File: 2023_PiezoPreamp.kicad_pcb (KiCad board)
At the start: 4 copper layers, 71 x 38 mm, 90 parts, among them J101 6.3mm stereo, J102 6.3mm stereo, J201 DC IN 5.5/2.1mm, J401 Spring Contact, U101 OPA145, U102 OPA145, U201 ZXMP3A17E6TA, U301 BC847BS,115

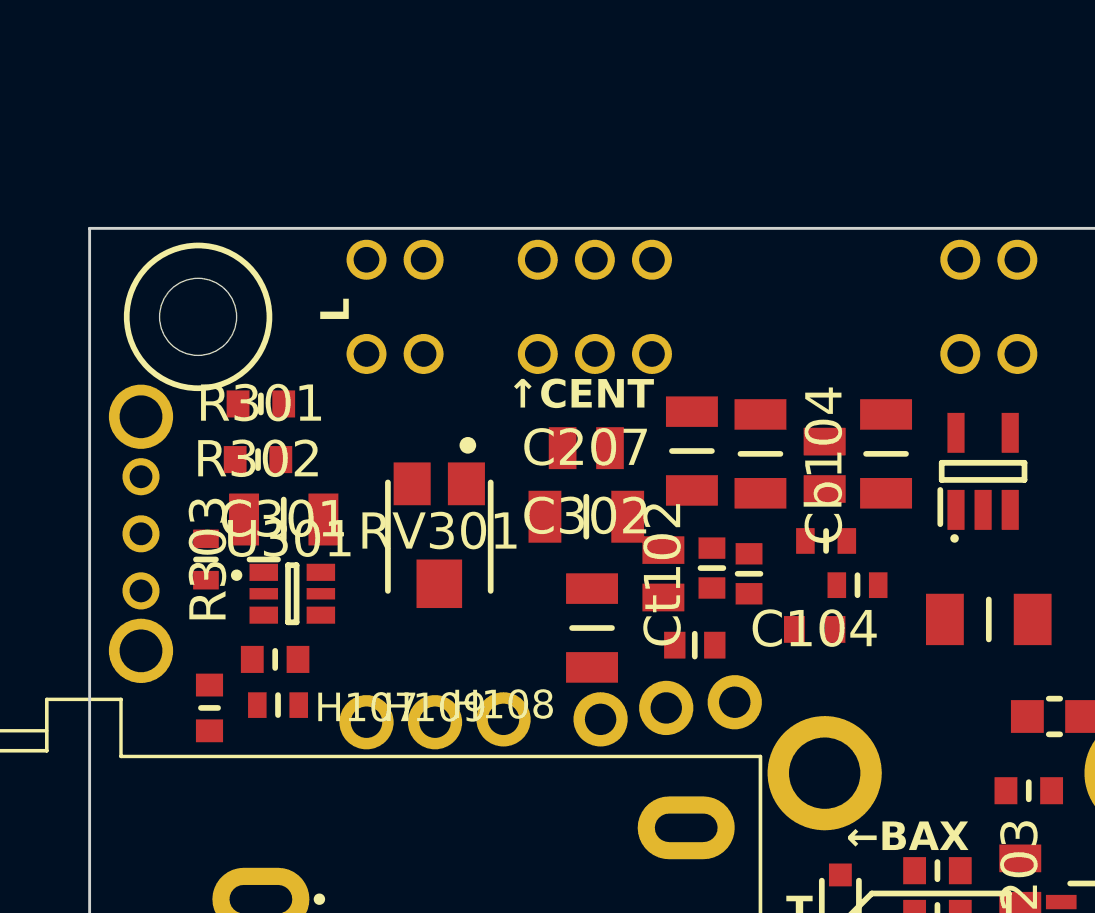
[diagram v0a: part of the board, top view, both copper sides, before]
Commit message: aligning schematics to grid, swapping switches as they are on the bottom side now; rough placement of BI section on board
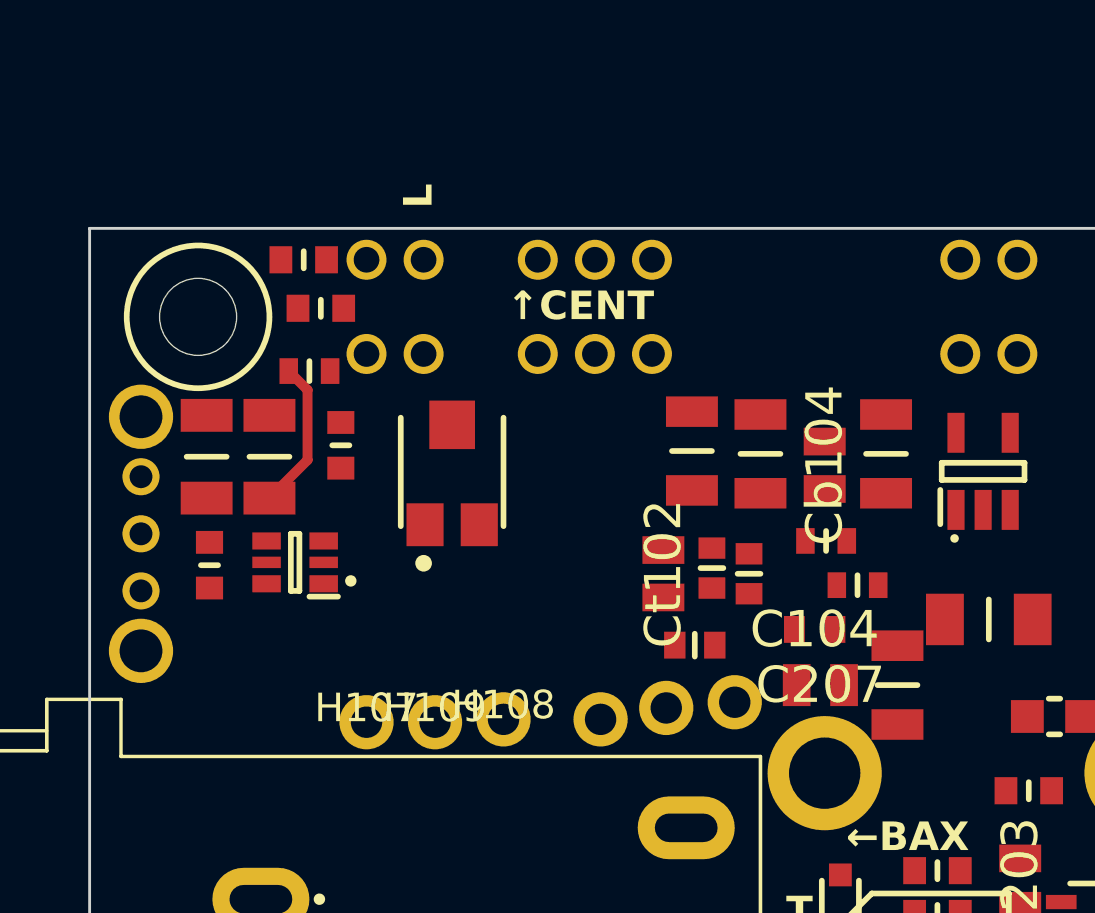
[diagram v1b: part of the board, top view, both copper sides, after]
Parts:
- removed the R304 at (121.5, 91.8)
- moved C207 11.7 mm to (140.5, 91.0)
- moved C302 11.3 mm to (121.2, 83.0), turned to -90 degrees
- moved C206 10.9 mm to (143.2, 91.0)
- moved R305 10.3 mm to (123.7, 82.7), turned to -90 degrees
- moved R303 7.53 mm to (122.6, 80.0), turned to 0 degrees
- moved R302 5.74 mm to (123.0, 77.8)
- moved R301 5.27 mm to (122.4, 76.2)
- moved R304 4.02 mm to (119.1, 86.8), turned to 90 degrees
- moved C301 3.48 mm to (119.0, 83.0), turned to -90 degrees
- moved RV301 2.31 mm to (127.6, 83.6), turned to 0 degrees
- moved U301 1.10 mm to (122.1, 86.8), turned to 180 degrees
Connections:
- Cb102 pad 1: /1-ChargeAmpAndEQ/C_SW_5 -> /1-ChargeAmpAndEQ/C_SW_1
- Cb103 pad 1: /1-ChargeAmpAndEQ/C_SW_4 -> /1-ChargeAmpAndEQ/C_SW_2
- Cb104 pad 1: /1-ChargeAmpAndEQ/C_SW_2 -> /1-ChargeAmpAndEQ/C_SW_4
- Cf102 pad 2: /1-ChargeAmpAndEQ/G_SW_6 -> /1-ChargeAmpAndEQ/G_SW_10
- Cf103 pad 2: /1-ChargeAmpAndEQ/G_SW_7 -> /1-ChargeAmpAndEQ/G_SW_9
- Cf104 pad 2: /1-ChargeAmpAndEQ/G_SW_7 -> /1-ChargeAmpAndEQ/G_SW_9
- Cf105 pad 2: /1-ChargeAmpAndEQ/G_SW_9 -> /1-ChargeAmpAndEQ/G_SW_7
- Cf106 pad 2: /1-ChargeAmpAndEQ/G_SW_10 -> /1-ChargeAmpAndEQ/G_SW_6
- Clp103 pad 1: /1-ChargeAmpAndEQ/LPF_SW_6 -> /1-ChargeAmpAndEQ/LPF_SW_10
- Clp104 pad 2: /1-ChargeAmpAndEQ/LPF_SW_7 -> /1-ChargeAmpAndEQ/LPF_SW_9
- Clp105 pad 2: /1-ChargeAmpAndEQ/LPF_SW_7 -> /1-ChargeAmpAndEQ/LPF_SW_9
- Clp106 pad 2: /1-ChargeAmpAndEQ/LPF_SW_9 -> /1-ChargeAmpAndEQ/LPF_SW_7
- Ct102 pad 2: /1-ChargeAmpAndEQ/C_SW_6 -> /1-ChargeAmpAndEQ/C_SW_10
- Ct103 pad 2: /1-ChargeAmpAndEQ/C_SW_7 -> /1-ChargeAmpAndEQ/C_SW_9
- Ct104 pad 2: /1-ChargeAmpAndEQ/C_SW_9 -> /1-ChargeAmpAndEQ/C_SW_7
- H101 pad 1: /1-ChargeAmpAndEQ/BA_1 -> /1-ChargeAmpAndEQ/BASS_1
- H102 pad 1: /1-ChargeAmpAndEQ/BA_2 -> /1-ChargeAmpAndEQ/BASS_2
- H103 pad 1: /1-ChargeAmpAndEQ/BA_3 -> /1-ChargeAmpAndEQ/BASS_3
- H104 pad 1: /1-ChargeAmpAndEQ/TR_1 -> /1-ChargeAmpAndEQ/TREB_1
- H105 pad 1: /1-ChargeAmpAndEQ/TR_2 -> /1-ChargeAmpAndEQ/TREB_2
- H106 pad 1: /1-ChargeAmpAndEQ/TR_3 -> /1-ChargeAmpAndEQ/TREB_3
- S102 pad 10: unconnected-(S102-Pad10) -> /1-ChargeAmpAndEQ/LPF_SW_10
- S102 pad 6: /1-ChargeAmpAndEQ/LPF_SW_6 -> unconnected-(S102-Pad6)
- S103 pad 1: unconnected-(S103-Pad1) -> /1-ChargeAmpAndEQ/C_SW_1
- S103 pad 10: unconnected-(S103-Pad10) -> /1-ChargeAmpAndEQ/C_SW_10
- S103 pad 5: /1-ChargeAmpAndEQ/C_SW_5 -> unconnected-(S103-Pad5)
- S103 pad 6: /1-ChargeAmpAndEQ/C_SW_6 -> unconnected-(S103-Pad6)
- S301 pad 1: unconnected-(S301-Pad1) -> /3-BatteryIndicator/BI_SW
- S301 pad 3: /3-BatteryIndicator/BI_SW -> unconnected-(S301-Pad3)
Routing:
- net /3-BatteryIndicator/BI_B1: track 0.00 -> 5.28 mm

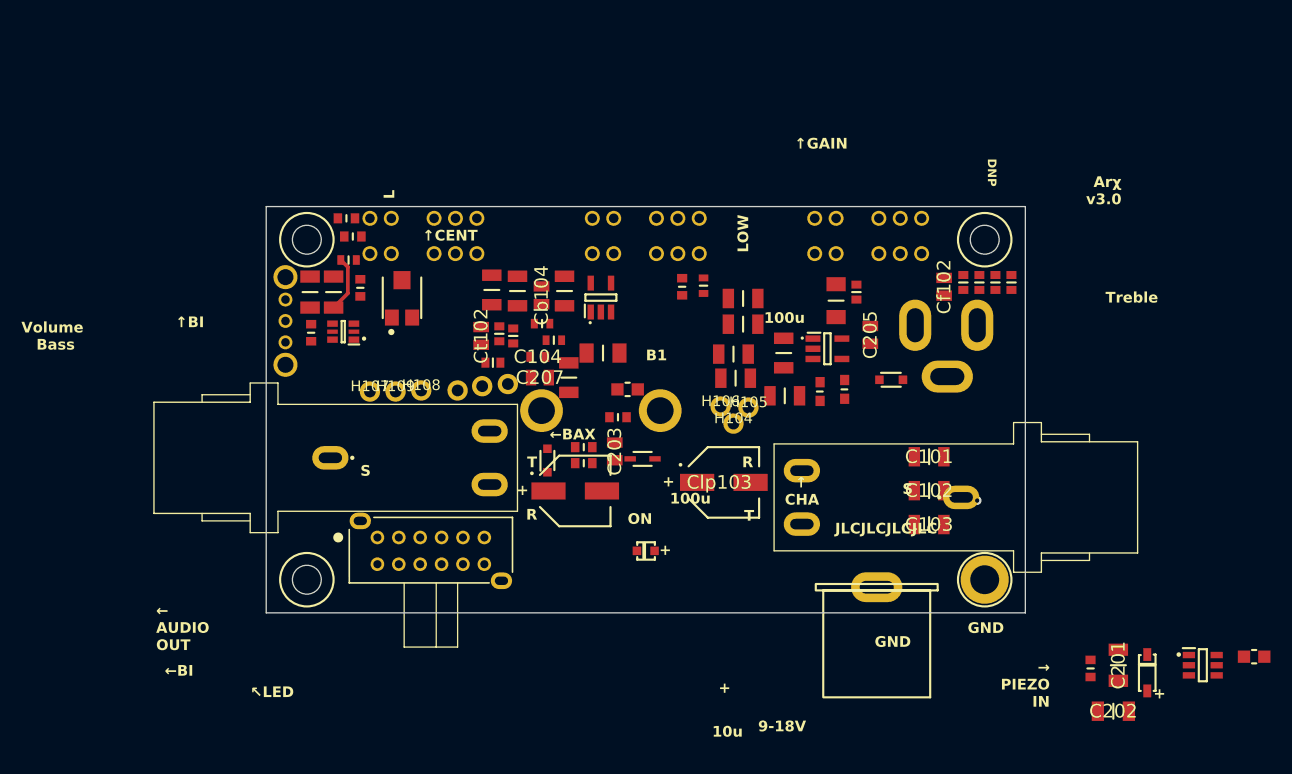
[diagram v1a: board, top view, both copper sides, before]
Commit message: PCB: updating all component footprints from schematics; starting some basic placement again
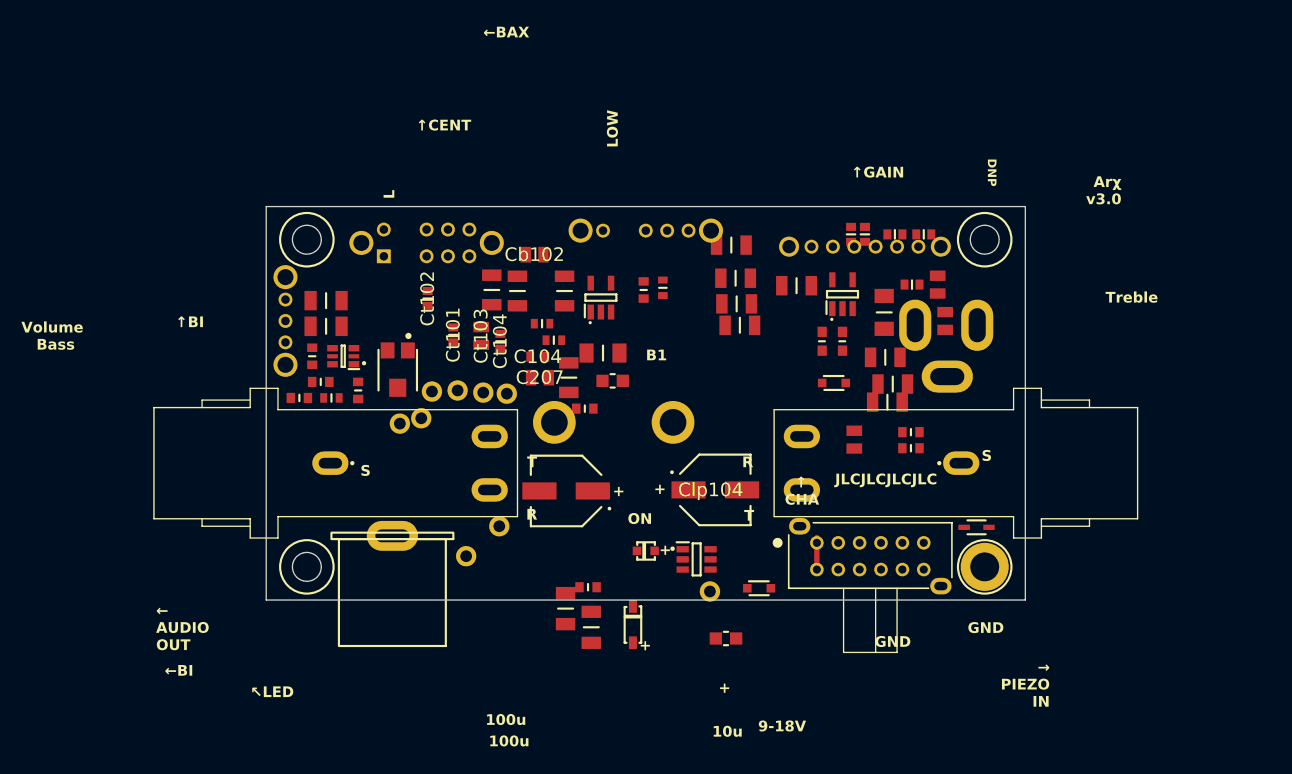
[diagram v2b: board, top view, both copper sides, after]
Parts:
- removed the Cb104 at (140.7, 83.3)
- removed the Clp104 at (159.5, 86.0)
- removed the Ct103 at (136.7, 87.0)
- added Cb102: 22n, library:GRM21B5C1H223JA01L, F.Cu at (140.0, 79.5)
- added Ct102: 4n7, library:GRM1885C1H472JA01D, F.Cu at (130.0, 83.7)
- Ct101: value 6n8 -> 4n7; footprint library:GRM1885C1H682JA01D -> library:GRM1885C1H472JA01D
- S101: value SSSS224100 -> SK14D01G6; footprint library:SSSS224100 -> library:sw_SK14D01G6
- S102: value SSSS224100 -> OS103011MA7QP1; footprint library:SSSS224100 -> library:sw_OS103011MA7QP1
- S103: value SSSS224100 -> 0S203011MA2QP1; footprint library:SSSS224100 -> library:sw_0S203011MA2QP1
- moved C202 52.1 mm to (142.9, 112.7), turned to -90 degrees
- moved R202 49.4 mm to (157.9, 115.5)
- moved C201 49.4 mm to (145.3, 114.4)
- moved U201 48.4 mm to (155.2, 108.0)
- moved D202 48.3 mm to (149.2, 114.2)
- moved R201 47.6 mm to (145.0, 110.7), turned to 180 degrees
- moved J401 45.6 mm to (126.7, 105.8)
- moved S201 41.1 mm to (171.4, 107.8)
- moved H108 32.9 mm to (156.4, 111.0)
- moved D201 31.9 mm to (181.3, 105.0), turned to 180 degrees
- moved R203 30.6 mm to (175.2, 96.2)
- moved R204 30.6 mm to (175.2, 97.7)
- moved H106 30.0 mm to (127.4, 95.3)
- moved H105 29.6 mm to (130.4, 92.3)
- moved H104 29.2 mm to (129.4, 94.8)
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- renumbered Cb102 to Cb103, Cb103 to Cb104, Clp106 to Clp103, Clp103 to Clp104, Ct102 to Ct103
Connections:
- net Net-(J201-SWITCH) renamed /2-Power/DC_IN_SW
- Cb101 pad 1: /1-ChargeAmpAndEQ/BA_1 -> /1-ChargeAmpAndEQ/BASS_3
- Cb101 pad 2: /1-ChargeAmpAndEQ/BA_3 -> /1-ChargeAmpAndEQ/BASS_1
- Cb103 pad 1: /1-ChargeAmpAndEQ/C_SW_1 -> /1-ChargeAmpAndEQ/C_SW_5
- Cb103 pad 2: /1-ChargeAmpAndEQ/BA_1 -> /1-ChargeAmpAndEQ/BASS_1
- Cb104 pad 1: /1-ChargeAmpAndEQ/C_SW_2 -> /1-ChargeAmpAndEQ/C_SW_7
- Cb104 pad 2: /1-ChargeAmpAndEQ/BA_1 -> /1-ChargeAmpAndEQ/BASS_1
- Cf102 pad 2: /1-ChargeAmpAndEQ/G_SW_10 -> /1-ChargeAmpAndEQ/G_SW_1
- Cf103 pad 2: /1-ChargeAmpAndEQ/G_SW_9 -> /1-ChargeAmpAndEQ/G_SW_2
- Cf104 pad 2: /1-ChargeAmpAndEQ/G_SW_9 -> /1-ChargeAmpAndEQ/G_SW_2
- Cf105 pad 2: /1-ChargeAmpAndEQ/G_SW_7 -> /1-ChargeAmpAndEQ/G_SW_5
- Clp103 pad 1: /1-ChargeAmpAndEQ/BAX_IN -> /1-ChargeAmpAndEQ/CH_A_OUT
- Clp103 pad 2: /1-ChargeAmpAndEQ/LPF_SW_7 -> /1-ChargeAmpAndEQ/BAX_IN
- Clp105 pad 2: /1-ChargeAmpAndEQ/LPF_SW_9 -> /1-ChargeAmpAndEQ/LPF_SW_3
- Ct101 pad 2: /1-ChargeAmpAndEQ/TR_2 -> /1-ChargeAmpAndEQ/TREB_2
- Ct103 pad 1: /1-ChargeAmpAndEQ/TR_2 -> /1-ChargeAmpAndEQ/TREB_2
- Ct103 pad 2: /1-ChargeAmpAndEQ/C_SW_10 -> /1-ChargeAmpAndEQ/C_SW_1
- Ct104 pad 1: /1-ChargeAmpAndEQ/TR_2 -> /1-ChargeAmpAndEQ/TREB_2
- Ct104 pad 2: /1-ChargeAmpAndEQ/C_SW_7 -> /1-ChargeAmpAndEQ/C_SW_2
- R103 pad 1: /1-ChargeAmpAndEQ/BA_2 -> /1-ChargeAmpAndEQ/BASS_2
- Rb101 pad 2: /1-ChargeAmpAndEQ/BA_3 -> /1-ChargeAmpAndEQ/BASS_3
- Rb102 pad 1: /1-ChargeAmpAndEQ/BA_1 -> /1-ChargeAmpAndEQ/BASS_1
- Rt101 pad 2: /1-ChargeAmpAndEQ/TR_3 -> /1-ChargeAmpAndEQ/TREB_3
- Rt102 pad 1: /1-ChargeAmpAndEQ/TR_1 -> /1-ChargeAmpAndEQ/TREB_1
- S101 pad 1: unconnected-(S101-Pad1) -> /1-ChargeAmpAndEQ/G_SW_1
- S101 pad 2: unconnected-(S101-Pad2) -> /1-ChargeAmpAndEQ/G_SW_2
- S101 pad 3: unconnected-(S101-Pad3) -> /1-ChargeAmpAndEQ/CH_A_OUT
- S101 pad 4: unconnected-(S101-Pad4) -> /1-ChargeAmpAndEQ/CH_A_OUT
- S101 pad 5: unconnected-(S101-Pad5) -> /1-ChargeAmpAndEQ/G_SW_5
- S102 pad 1: unconnected-(S102-Pad1) -> /1-ChargeAmpAndEQ/LPF_SW_10
- S102 pad 2: unconnected-(S102-Pad2) -> /1-ChargeAmpAndEQ/CH_A_OUT
- S102 pad 3: unconnected-(S102-Pad3) -> /1-ChargeAmpAndEQ/LPF_SW_3
- S103 pad 2: /1-ChargeAmpAndEQ/C_SW_2 -> /1-ChargeAmpAndEQ/BAX_A_INV
- S103 pad 3: /1-ChargeAmpAndEQ/BA_3 -> /1-ChargeAmpAndEQ/C_SW_2
- S103 pad 4: /1-ChargeAmpAndEQ/C_SW_4 -> unconnected-(S103-2_3-Pad4)
- S103 pad 5: unconnected-(S103-Pad5) -> /1-ChargeAmpAndEQ/C_SW_5
- S103 pad 6: unconnected-(S103-Pad6) -> /1-ChargeAmpAndEQ/BASS_3
- S103 pad 8: /1-ChargeAmpAndEQ/BAX_A_INV -> unconnected-(S103-1_3-Pad8)
- S201 pad 11: /2-Power/DC_IN_ESD -> unconnected-(S201-Pad11)
- S201 pad 12: /2-Power/DC_IN_POS -> unconnected-(S201-Pad12)
- S201 pad 5: unconnected-(S201-Pad5) -> /2-Power/DC_IN_ESD
- S201 pad 6: unconnected-(S201-Pad6) -> /2-Power/DC_IN_POS
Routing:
- net /3-BatteryIndicator/BI_B1: track 5.28 -> 0.00 mm
- net /2-Power/BYPASS: track 0.00 -> 2.50 mm
- net GND: vias 1 -> 0
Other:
- board size 71 x 38 mm -> 71 x 36.8 mm
- board text added: "loose jack Y = 27.2"
- board text removed: "jack Y = 27.2"

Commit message: updating the board and remaining low-pass references in schematic
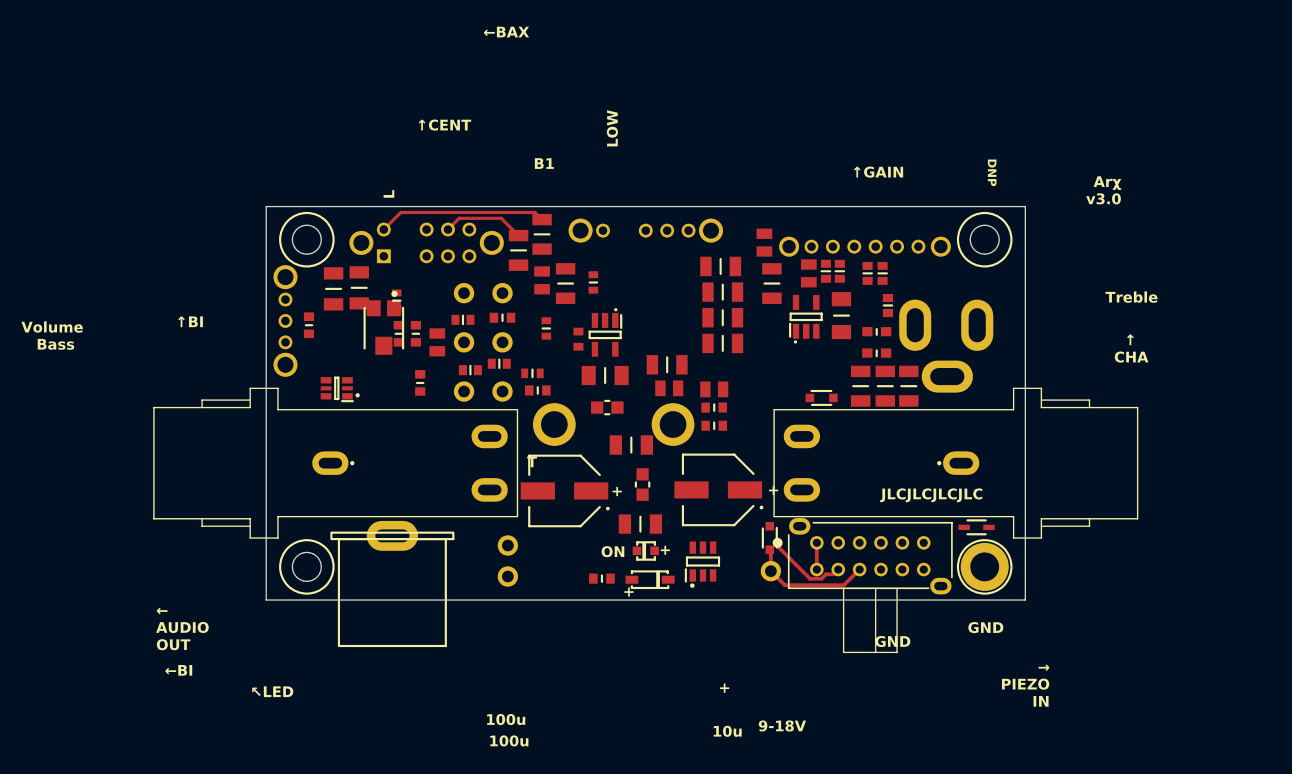
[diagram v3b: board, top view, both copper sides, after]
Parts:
- moved R204 18.8 mm to (156.8, 93.8)
- moved C205 18.4 mm to (161.5, 78.4), turned to -90 degrees
- moved R203 18.4 mm to (156.8, 95.5)
- moved C202 16.5 mm to (149.1, 97.3), turned to 0 degrees
- moved R202 16.4 mm to (150.1, 101.0), turned to -90 degrees
- moved C203 13.9 mm to (156.8, 92.2), turned to 0 degrees
- moved H106 13.6 mm to (133.4, 83.2)
- moved Rt101 13.5 mm to (137.0, 85.5), turned to 180 degrees
- moved R301 12.4 mm to (128.9, 87.0), turned to 90 degrees
- moved C207 12.1 mm to (152.6, 92.0)
- moved Cf102 12.1 mm to (165.7, 81.3)
- moved Rb101 11.5 mm to (141.1, 86.5), turned to -90 degrees
- moved R303 11.0 mm to (127.1, 83.8), turned to -90 degrees
- moved C201 10.7 mm to (149.9, 104.8), turned to 0 degrees
- moved H101 9.47 mm to (137.0, 83.2)
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- renumbered Clp101 to Chp101, Clp102 to Chp102, Clp103 to Chp103, Clp104 to Chp104, Clp105 to Chp105
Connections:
- net /1-ChargeAmpAndEQ/LPF_SW_10 renamed /1-ChargeAmpAndEQ/HPF_SW_10
- net /1-ChargeAmpAndEQ/LPF_SW_3 renamed /1-ChargeAmpAndEQ/HPF_SW_3
- S201 pad 11: unconnected-(S201-Pad11) -> /2-Power/DC_IN_ESD
- S201 pad 12: unconnected-(S201-Pad12) -> /2-Power/DC_IN_POS
- S201 pad 5: /2-Power/DC_IN_ESD -> unconnected-(S201-Pad5)
- S201 pad 6: /2-Power/DC_IN_POS -> unconnected-(S201-Pad6)
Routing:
- net /1-ChargeAmpAndEQ/C_SW_5: track 0.00 -> 15.7 mm
- net AUDIO_ESD: track 0.00 -> 11.5 mm
- net /1-ChargeAmpAndEQ/C_SW_7: track 0.00 -> 7.71 mm
- net AUDIO_OUT: track 0.00 -> 7.21 mm
